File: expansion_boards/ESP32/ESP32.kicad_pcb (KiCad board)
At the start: 2 copper layers, 51 x 26 mm, 19 parts, among them J4 OLED, SW1 GPIO0, SW2 RESET, U1 ESP32-WROOM-32E

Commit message: Update Expansion board
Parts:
- removed kibuzzard-6431D11C-2: G009, kibuzzard-6431D11C-2
- added kibuzzard-68375C5E: G***, kibuzzard-68375C5E, B.Cu at (76.1, 42.6)
- moved G004 0.20 mm to (84.1, 56.8)
- moved kibuzzard-64EB6544-2 0.20 mm to (76.1, 47.0)
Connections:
- net /RFM_MISO renamed /RFM_MISO/D12
- net /RFM_MOSI renamed /RFM_MOSI/D11
- net /RFM_SCK renamed /RFM_SCK/D13
- net /RFM_SEL renamed /RFM_SEL/D10
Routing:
- net GND: vias 20 -> 65
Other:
- board text added: "Mk2PVRouter ESP32 Expansion Board"
- board text removed: "Mk2PVRouter Expansion Board"

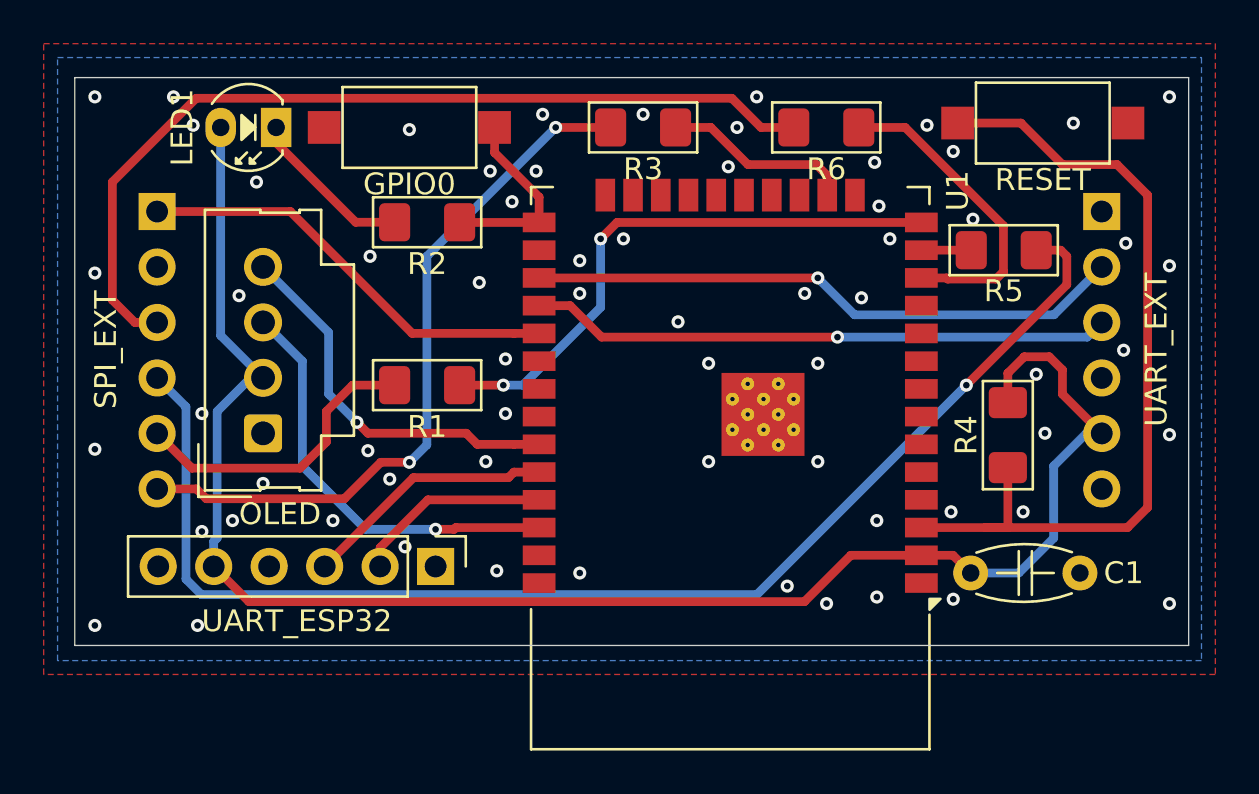
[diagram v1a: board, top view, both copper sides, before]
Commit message: Add AP2112R5A-3.3TRG1 3D model and update KiCad files
Added the AP2112R5A-3.3TRG1 STEP 3D model. Updated ESP32 and 3phaseDiverter KiCad project, schematic, PCB, and design rule files, including the addition of a new design rules file for the ESP32 board.
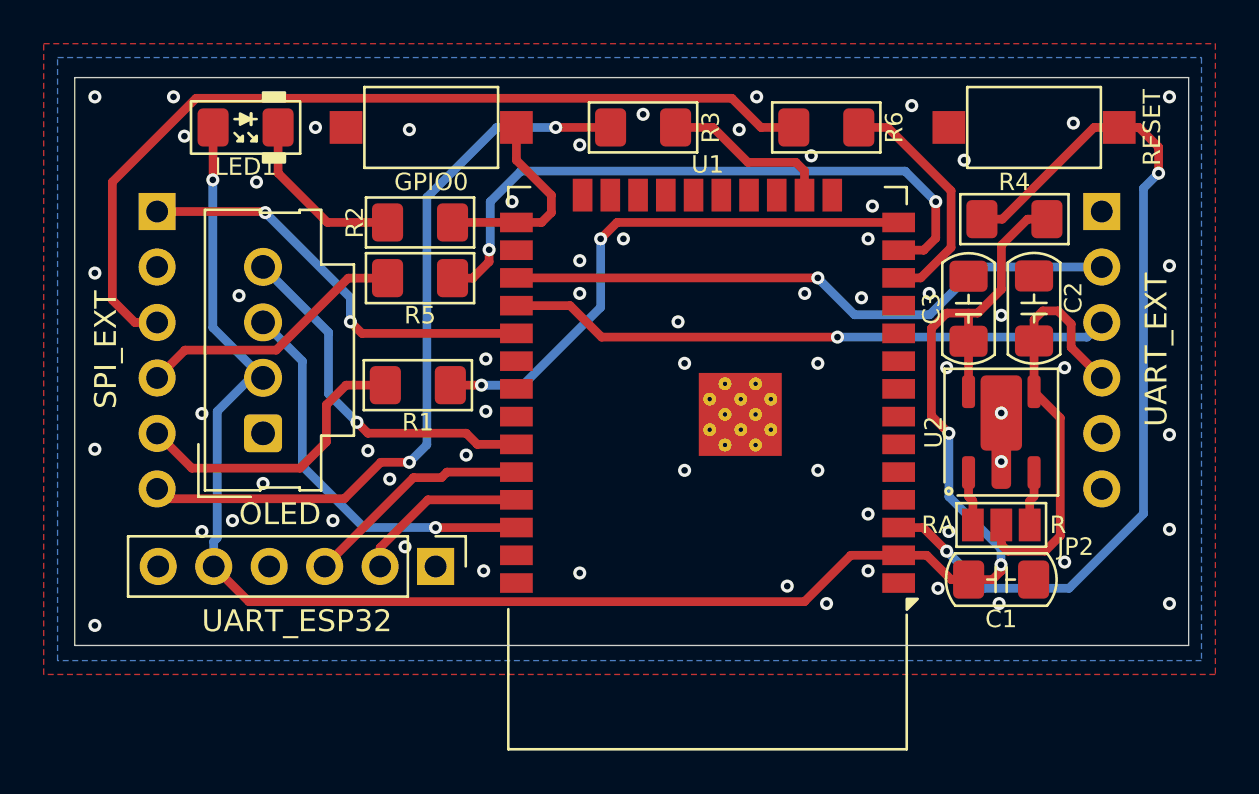
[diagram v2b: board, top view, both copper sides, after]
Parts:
- added C2: 4u7, PCM_Capacitor_SMD_Handsoldering_AKL:C_1206_3216Metric_Pad1.42x1.75mm, F.Cu at (94.5, 50.8)
- added C3: 4u7, PCM_Capacitor_SMD_Handsoldering_AKL:C_1206_3216Metric_Pad1.42x1.75mm, F.Cu at (91.5, 50.8)
- added JP2: SolderJumper_3_Open, Jumper:SolderJumper-3_P1.3mm_Open_Pad1.0x1.5mm_NumberLabels, F.Cu at (93.0, 60.7)
- added U2: AP2112R5-3.3TRG1, PCM_Package_TO_SOT_SMD_AKL:Diodes_SOT-89-5, F.Cu at (93.0, 56.5)
- C1: value 10uF -> 100nF; footprint PCM_Capacitor_THT_AKL:C_Disc_D4.7mm_W2.5mm_P5.00mm -> PCM_Capacitor_SMD_Handsoldering_AKL:C_1206_3216Metric_Pad1.42x1.75mm
- LED1: value LED_3mm -> LED; footprint PCM_LED_THT_AKL:LED_D3.0mm -> PCM_LED_SMD_Handsoldering_AKL:LED_1206_3216Metric_Pad1.42x1.75mm
- moved R5 26.8 mm to (66.4, 49.4), turned to 180 degrees
- moved R4 9.89 mm to (93.6, 46.7), turned to 0 degrees
- moved C1 1.42 mm to (93.0, 63.2)
- moved LED1 1.40 mm to (58.4, 42.5)
- moved U1 1.04 mm to (79.5, 55.1)
- moved SW1 1.00 mm to (66.9, 42.5)
- moved SW2 0.45 mm to (94.5, 42.5), turned to 0 degrees
- moved R1 0.43 mm to (66.3, 54.3)
- moved R2 0.33 mm to (66.4, 46.9)
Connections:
- C1 pad 1: +3.3V -> +3V3
- J4 pad 2: +3.3V -> +3V3
- JP1 pad 5: +3.3V -> +3V3
- JP3 pad 4: unconnected-(JP3-Pin_4-Pad4) -> +5V
- JP3 pad 5: +3.3V -> unconnected-(JP3-Pin_5-Pad5)
- LED1 pad 2: +3.3V -> +3V3
- R4 pad 2: +3.3V -> +3V3
- U1 pad 2: +3.3V -> +3V3
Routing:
- net +3V3: track 0.00 -> 85.1 mm, vias 0 -> 3
- net +3.3V: track 77.4 -> 0.00 mm
- net /RFM_SCK/D13: track 59.1 -> 12.4 mm, vias 1 -> 0
- net Net-(U1-IO14): track 2.28 -> 29.9 mm, vias 0 -> 2
- net +5V: track 0.00 -> 19.6 mm
- net Net-(U1-IO27): track 14.5 -> 11.0 mm
- net Net-(JP2-B): track 0.00 -> 2.48 mm
- net Net-(JP2-A): track 0.00 -> 2.48 mm
- net /RESET: track 38.9 -> 41.1 mm, vias 0 -> 2
- net /RFM_MOSI/D11: track 33.0 -> 34.6 mm
- net /SCL: track 19.4 -> 18.3 mm
- net /ESP_RX: track 11.6 -> 10.6 mm
- net /SDA: track 17.7 -> 16.6 mm
- net /ESP_TX: track 9.05 -> 8.01 mm
- net /AVR_TX: track 27.4 -> 28.4 mm
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
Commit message: Update ESP32 board UART connector and net assignments
Replaced JP1 pin header with pin socket, changed its position and orientation, and updated net assignments for UART pins. Adjusted net indices throughout the PCB to match schematic changes, updated silkscreen and fab layer properties, and modified JP3 socket position and labeling for consistency.
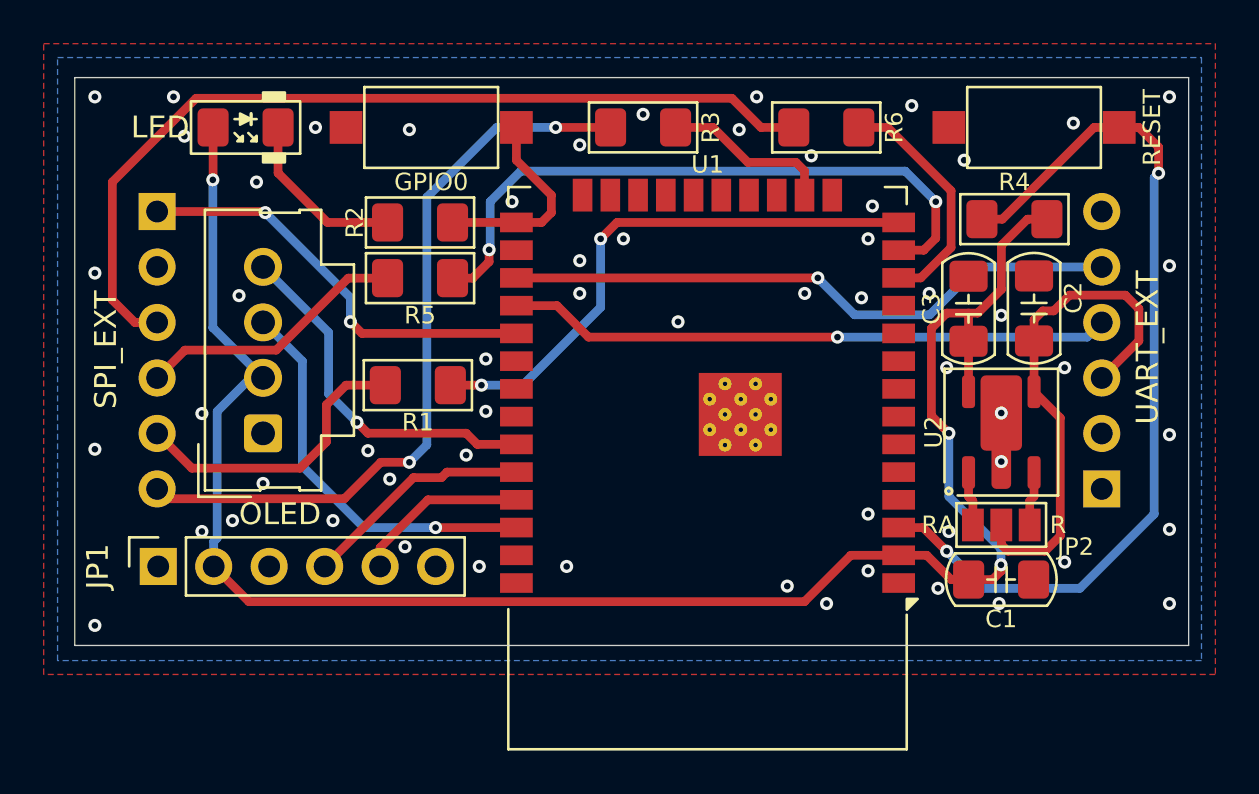
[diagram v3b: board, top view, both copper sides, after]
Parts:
- JP1: footprint Connector_PinHeader_2.54mm:PinHeader_1x06_P2.54mm_Vertical -> Connector_PinSocket_2.54mm:PinSocket_1x06_P2.54mm_Vertical
- moved JP1 12.7 mm to (54.4, 62.6), turned to 90 degrees
- moved JP3 12.7 mm to (97.6, 59.0), turned to 0 degrees
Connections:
- JP1 pad 1: unconnected-(JP1-Pin_1-Pad1) -> GND
- JP1 pad 2: /ESP_TX -> +3V3
- JP1 pad 3: /ESP_RX -> unconnected-(JP1-Pin_3-Pad3)
- JP1 pad 4: unconnected-(JP1-Pin_4-Pad4) -> /ESP_RX
- JP1 pad 5: +3V3 -> /ESP_TX
- JP1 pad 6: GND -> unconnected-(JP1-Pin_6-Pad6)
- JP3 pad 1: unconnected-(JP3-Pin_1-Pad1) -> GND
- JP3 pad 2: /AVR_TX -> unconnected-(JP3-Pin_2-Pad2)
- JP3 pad 3: /AVR_RX -> +5V
- JP3 pad 4: +5V -> /AVR_RX
- JP3 pad 5: unconnected-(JP3-Pin_5-Pad5) -> /AVR_TX
- JP3 pad 6: GND -> unconnected-(JP3-Pin_6-Pad6)
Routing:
- net +5V: track 19.6 -> 23.8 mm
- net GND: vias 63 -> 59
